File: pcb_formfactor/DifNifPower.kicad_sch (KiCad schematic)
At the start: 25 parts, among them U1 ICE40HX4K-TQ144, U3 APX803S00-29SA-7, U4 AP2114HA-3.3, U5 AP2114HA-1.2

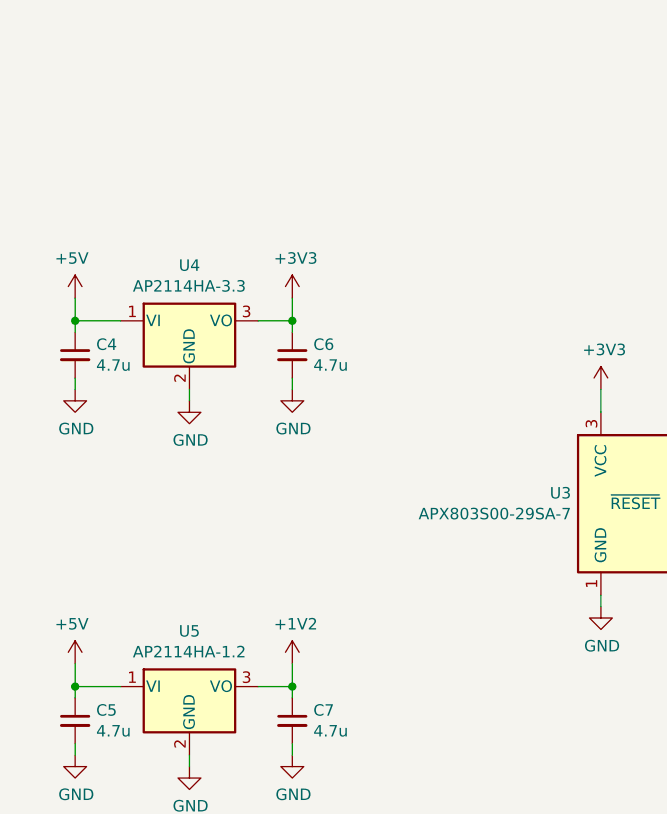
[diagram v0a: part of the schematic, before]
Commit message: Add diode OR, add clock series R
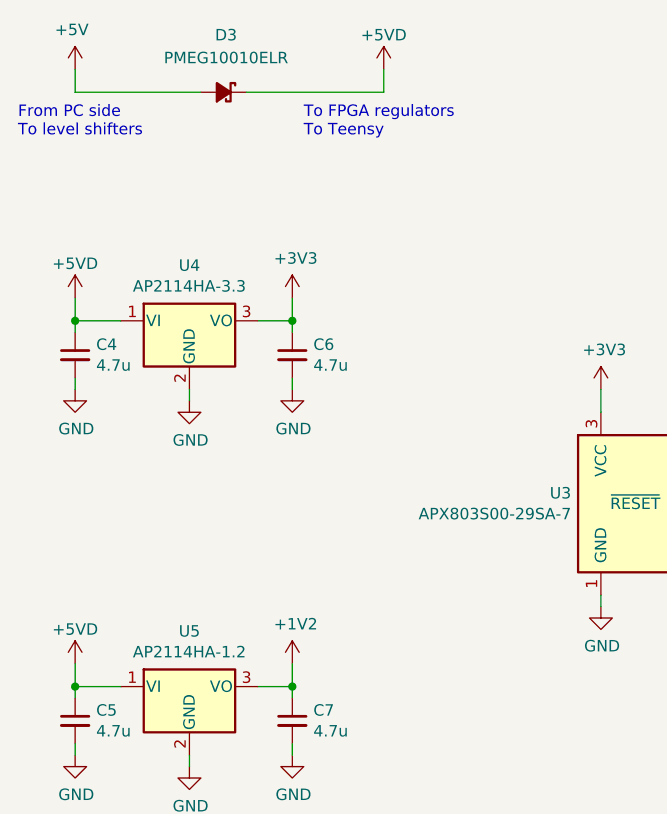
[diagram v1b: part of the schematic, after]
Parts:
- added D3: PMEG10010ELR, Active:SOD3716X117, symbol Device:D_Schottky_Small_Filled
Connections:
- net +5V: now also D3.2 (A); no longer C4.1, C5.1, U4.1 (VI), U5.1 (VI)
- new net +5VD: C4.1, C5.1, D3.1 (K), U4.1 (VI), U5.1 (VI)
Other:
- note added: "From PC side To level shifters"
- note added: "To FPGA regulators To Teensy"
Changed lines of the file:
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@@
+    (stroke (width 0) (type default) (color 0 0 0 0))
+  )
+  (wire (pts (xy 57.15 30.48) (xy 72.39 30.48))
     (stroke (width 0) (type default) (color 0 0 0 0))
   )
@@
     (stroke (width 0) (type default) (color 0 0 0 0))
   )
+  (wire (pts (xy 38.1 30.48) (xy 38.1 27.94))
+    (stroke (width 0) (type default) (color 0 0 0 0))
+  )
   (wire (pts (xy 138.43 114.3) (xy 130.81 114.3))
     (stroke (width 0) (type default) (color 0 0 0 0))
@@
     (stroke (width 0) (type default) (color 0 0 0 0))
   )
+  (wire (pts (xy 72.39 27.94) (xy 72.39 30.48))
+    (stroke (width 0) (type default) (color 0 0 0 0))
+  )
   (wire (pts (xy 214.63 129.54) (xy 199.39 129.54))
     (stroke (width 0) (type default) (color 0 0 0 0))
@@
   )
   (wire (pts (xy 38.1 96.52) (xy 38.1 97.79))
+    (stroke (width 0) (type default) (color 0 0 0 0))
+  )
+  (wire (pts (xy 52.07 30.48) (xy 38.1 30.48))
     (stroke (width 0) (type default) (color 0 0 0 0))
   )
@@
     (effects (font (size 1.27 1.27)) (justify left bottom))
   )
+  (text "To FPGA regulators\nTo Teensy" (at 63.5 35.56 0)
+    (effects (font (size 1.27 1.27)) (justify left bottom))
+  )
   (text "CONFIG TIME:\n230ms (slow, default)\n110ms (medium)\n70ms (fast)"
     (at 219.71 68.58 0)
@@
     (effects (font (size 1.27 1.27)) (justify left bottom))
   )
+  (text "From PC side\nTo level shifters" (at 31.75 35.56 0)
+    (effects (font (size 1.27 1.27)) (justify left bottom))
+  )
   (text "0.4V/ms to 10V/ms ramp rate range" (at 138.43 151.13 0)
     (effects (font (size 1.27 1.27)) (justify left bottom))
@@
     (pin "1")
   )
-  (symbol (lib_id "power:+5V") (at 38.1 93.98 0) (mirror y) (unit 1)
-    (in_bom yes) (on_board yes)
-    (property "Reference" "#PWR0116" (id 0) (at 38.1 97.79 0)
-      (effects (font (size 1.27 1.27)) hide)
-    )
-    (property "Value" "+5V" (id 1) (at 37.719 89.5858 0))
-    (property "Footprint" "" (id 2) (at 38.1 93.98 0)
-      (effects (font (size 1.27 1.27)) hide)
-    )
-    (property "Datasheet" "" (id 3) (at 38.1 93.98 0)
-      (effects (font (size 1.27 1.27)) hide)
-    )
-    (pin "1")
-  )
   (symbol (lib_id "Device:R_Small_US") (at 107.95 68.58 0) (unit 1)
     (in_bom yes) (on_board yes)
@@
     (pin "1")
     (pin "2")
-  )
-  (symbol (lib_id "power:+5V") (at 38.1 53.34 0) (mirror y) (unit 1)
-    (in_bom yes) (on_board yes)
-    (property "Reference" "#PWR0119" (id 0) (at 38.1 57.15 0)
-      (effects (font (size 1.27 1.27)) hide)
-    )
-    (property "Value" "+5V" (id 1) (at 37.719 48.9458 0))
-    (property "Footprint" "" (id 2) (at 38.1 53.34 0)
-      (effects (font (size 1.27 1.27)) hide)
-    )
-    (property "Datasheet" "" (id 3) (at 38.1 53.34 0)
-      (effects (font (size 1.27 1.27)) hide)
-    )
-    (pin "1")
   )
   (symbol (lib_id "Device:C_Small") (at 173.99 135.89 0) (unit 1)
@@
     (pin "1")
   )
+  (symbol (lib_id "power:+5VD") (at 38.1 93.98 0) (unit 1)
+    (in_bom yes) (on_board yes)
+    (property "Reference" "#PWR019" (id 0) (at 38.1 97.79 0)
+      (effects (font (size 1.27 1.27)) hide)
+    )
+    (property "Value" "+5VD" (id 1) (at 38.1 90.17 0))
+    (property "Footprint" "" (id 2) (at 38.1 93.98 0)
+      (effects (font (size 1.27 1.27)) hide)
+    )
+    (property "Datasheet" "" (id 3) (at 38.1 93.98 0)
+      (effects (font (size 1.27 1.27)) hide)
+    )
+    (pin "1")
+  )
   (symbol (lib_id "power:+1V2") (at 207.01 113.03 0) (unit 1)
     (in_bom yes) (on_board yes)
@@
     (pin "1")
   )
+  (symbol (lib_id "power:+5VD") (at 38.1 53.34 0) (unit 1)
+    (in_bom yes) (on_board yes)
+    (property "Reference" "#PWR018" (id 0) (at 38.1 57.15 0)
+      (effects (font (size 1.27 1.27)) hide)
+    )
+    (property "Value" "+5VD" (id 1) (at 38.1 49.53 0))
+    (property "Footprint" "" (id 2) (at 38.1 53.34 0)
+      (effects (font (size 1.27 1.27)) hide)
+    )
+    (property "Datasheet" "" (id 3) (at 38.1 53.34 0)
+      (effects (font (size 1.27 1.27)) hide)
+    )
+    (pin "1")
+  )
   (symbol (lib_id "Power_Supervisor:TCM809") (at 99.06 76.2 0) (unit 1)
     (in_bom yes) (on_board yes)
@@
     (pin "3")
   )
+  (symbol (lib_id "Device:D_Schottky_Small_Filled") (at 54.61 30.48 0) (mirror y) (unit 1)
+    (in_bom yes) (on_board yes) (fields_autoplaced)
+    (property "Reference" "D3" (id 0) (at 54.864 24.13 0))
+    (property "Value" "PMEG10010ELR" (id 1) (at 54.864 26.67 0))
+    (property "Footprint" "Active:SOD3716X117" (id 2) (at 54.61 30.48 90)
+      (effects (font (size 1.27 1.27)) hide)
+    )
+    (property "Datasheet" "~" (id 3) (at 54.61 30.48 90)
+      (effects (font (size 1.27 1.27)) hide)
+    )
+    (property "Mouser" "771-PMEG10010ELRX" (id 4) (at 54.61 30.48 0)
+      (effects (font (size 1.27 1.27)) hide)
+    )
+    (pin "1")
+    (pin "2")
+  )
   (symbol (lib_id "Device:C_Small") (at 194.31 86.36 0) (unit 1)
     (in_bom yes) (on_board yes)
@@
     (pin "1")
     (pin "2")
+  )
+  (symbol (lib_id "power:+5VD") (at 72.39 27.94 0) (unit 1)
+    (in_bom yes) (on_board yes)
+    (property "Reference" "#PWR020" (id 0) (at 72.39 31.75 0)
+      (effects (font (size 1.27 1.27)) hide)
+    )
+    (property "Value" "+5VD" (id 1) (at 72.39 24.13 0))
+    (property "Footprint" "" (id 2) (at 72.39 27.94 0)
+      (effects (font (size 1.27 1.27)) hide)
+    )
+    (property "Datasheet" "" (id 3) (at 72.39 27.94 0)
+      (effects (font (size 1.27 1.27)) hide)
+    )
+    (pin "1")
   )
   (symbol (lib_id "Device:C_Small") (at 207.01 118.11 0) (unit 1)
@@
     (pin "2")
   )
+  (symbol (lib_id "power:+5V") (at 38.1 27.94 0) (mirror y) (unit 1)
+    (in_bom yes) (on_board yes)
+    (property "Reference" "#PWR017" (id 0) (at 38.1 31.75 0)
+      (effects (font (size 1.27 1.27)) hide)
+    )
+    (property "Value" "+5V" (id 1) (at 37.719 23.5458 0))
+    (property "Footprint" "" (id 2) (at 38.1 27.94 0)
+      (effects (font (size 1.27 1.27)) hide)
+    )
+    (property "Datasheet" "" (id 3) (at 38.1 27.94 0)
+      (effects (font (size 1.27 1.27)) hide)
+    )
+    (pin "1")
+  )
   (symbol (lib_id "Device:C_Small") (at 199.39 135.89 0) (unit 1)
